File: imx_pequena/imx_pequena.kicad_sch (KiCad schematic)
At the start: 0 parts

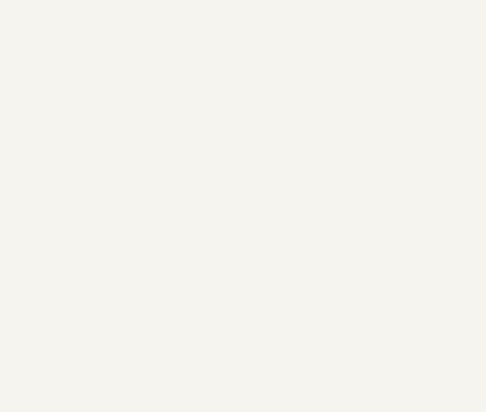
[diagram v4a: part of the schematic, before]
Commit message: Pinout updates
Updated pinout files, changed pinout of gpio 1 and 3
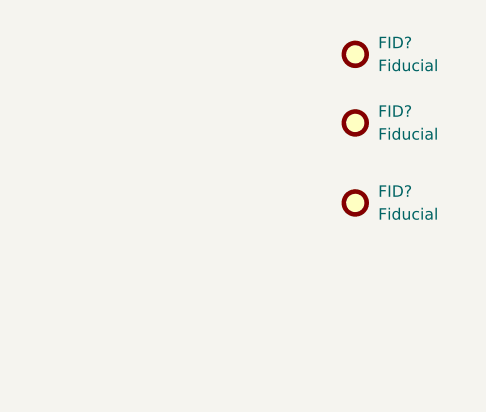
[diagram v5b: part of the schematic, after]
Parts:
- added FID? (x3): Fiducial, symbol Mechanical:Fiducial
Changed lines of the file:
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@@
     (stroke (width 0) (type default) (color 0 0 0 0))
+  )
+  (symbol (lib_id "Mechanical:Fiducial") (at 179.07 77.47 0) (unit 1)
+    (in_bom yes) (on_board yes) (fields_autoplaced)
+    (property "Reference" "FID?" (id 0) (at 181.61 76.1999 0)
+      (effects (font (size 1.27 1.27)) (justify left))
+    )
+    (property "Value" "Fiducial" (id 1) (at 181.61 78.7399 0)
+      (effects (font (size 1.27 1.27)) (justify left))
+    )
+    (property "Footprint" "" (id 2) (at 179.07 77.47 0)
+      (effects (font (size 1.27 1.27)) hide)
+    )
+    (property "Datasheet" "~" (id 3) (at 179.07 77.47 0)
+      (effects (font (size 1.27 1.27)) hide)
+    )
+  )
+  (symbol (lib_id "Mechanical:Fiducial") (at 179.07 86.36 0) (unit 1)
+    (in_bom yes) (on_board yes) (fields_autoplaced)
+    (property "Reference" "FID?" (id 0) (at 181.61 85.0899 0)
+      (effects (font (size 1.27 1.27)) (justify left))
+    )
+    (property "Value" "Fiducial" (id 1) (at 181.61 87.6299 0)
+      (effects (font (size 1.27 1.27)) (justify left))
+    )
+    (property "Footprint" "" (id 2) (at 179.07 86.36 0)
+      (effects (font (size 1.27 1.27)) hide)
+    )
+    (property "Datasheet" "~" (id 3) (at 179.07 86.36 0)
+      (effects (font (size 1.27 1.27)) hide)
+    )
+  )
+  (symbol (lib_id "Mechanical:Fiducial") (at 179.07 69.85 0) (unit 1)
+    (in_bom yes) (on_board yes) (fields_autoplaced)
+    (property "Reference" "FID?" (id 0) (at 181.61 68.5799 0)
+      (effects (font (size 1.27 1.27)) (justify left))
+    )
+    (property "Value" "Fiducial" (id 1) (at 181.61 71.1199 0)
+      (effects (font (size 1.27 1.27)) (justify left))
+    )
+    (property "Footprint" "" (id 2) (at 179.07 69.85 0)
+      (effects (font (size 1.27 1.27)) hide)
+    )
+    (property "Datasheet" "~" (id 3) (at 179.07 69.85 0)
+      (effects (font (size 1.27 1.27)) hide)
+    )
   )
   (sheet (at 54.61 100.33) (size 33.02 20.32) (fields_autoplaced)
@@
       (reference "#PWR?") (unit 1) (value "GND") (footprint "")
     )
+    (path "/e35c56f9-4713-4571-acdb-6ae2f2073fad/19abf78c-447d-4a26-a146-68b25d9e4c7a"
+      (reference "#PWR?") (unit 1) (value "GND") (footprint "")
+    )
     (path "/b1ca3e0b-34ce-4229-a1de-c4269e4ccd13/e4b0b1c3-ef5e-4ab5-8d70-6acfd00108e3/27f72761-f65f-4e29-a308-3170c5b56d4e"
       (reference "#PWR?") (unit 1) (value "GND") (footprint "")
@@
       (reference "D2") (unit 1) (value "D_Schottky") (footprint "")
     )
+    (path "/e35c56f9-4713-4571-acdb-6ae2f2073fad/24569c5c-3905-42a7-b371-b23bc9cdaa9e"
+      (reference "D?") (unit 1) (value "D_TVS") (footprint "")
+    )
     (path "/b1ca3e0b-34ce-4229-a1de-c4269e4ccd13/e4b0b1c3-ef5e-4ab5-8d70-6acfd00108e3/f018a515-bdc2-4719-84b3-f29126a0bfa9"
       (reference "D?") (unit 1) (value "D_Schottky") (footprint "")
@@
       (reference "F?") (unit 1) (value "Fuse_Small") (footprint "")
     )
+    (path "/64e54a22-63a0-4db2-b405-8a28a973ed5d"
+      (reference "FID?") (unit 1) (value "Fiducial") (footprint "")
+    )
+    (path "/b6dfcf66-fbe6-453a-a92a-d4357889378e"
+      (reference "FID?") (unit 1) (value "Fiducial") (footprint "")
+    )
+    (path "/c3797c65-0eba-45f0-a5bc-5a86e83cb0c5"
+      (reference "FID?") (unit 1) (value "Fiducial") (footprint "")
+    )
     (path "/b1ca3e0b-34ce-4229-a1de-c4269e4ccd13/e4b0b1c3-ef5e-4ab5-8d70-6acfd00108e3/af73b285-838d-4b82-83cb-376f8bbe2ef4"
       (reference "J1") (unit 1) (value "Conn_ARM_JTAG_SWD_10") (footprint "")
@@
       (reference "J2") (unit 1) (value "Micro_SD_Card") (footprint "")
     )
-    (path "/e35c56f9-4713-4571-acdb-6ae2f2073fad/f26dfe91-6ea2-4dd7-ac27-80f43cf12e1c"
-      (reference "J3") (unit 1) (value "USB_B_Micro") (footprint "")
-    )
     (path "/e35c56f9-4713-4571-acdb-6ae2f2073fad/e117ef28-5c52-4d5c-bd4e-b5be24785834"
       (reference "J4") (unit 1) (value "USB_C_Receptacle") (footprint "")
     )
+    (path "/e35c56f9-4713-4571-acdb-6ae2f2073fad/b8dbd3c7-4df0-4d11-8ddd-ea24cb3f2676"
+      (reference "J?") (unit 1) (value "USB_A") (footprint "")
+    )
     (path "/08944c63-1cea-4fda-90db-3d649a3edc95/9ee5e8f1-d628-4347-87c6-e91ba1bc0c3e"

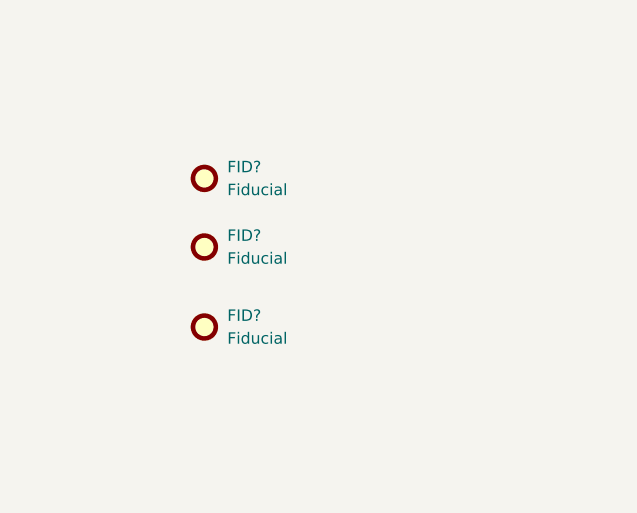
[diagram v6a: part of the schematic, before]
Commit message: Part Assignment
Assigned GPIOs and assigned footprints to most parts
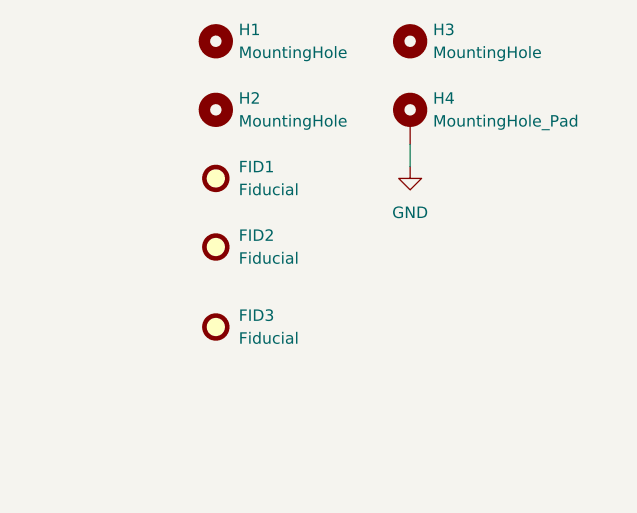
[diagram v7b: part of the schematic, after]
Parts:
- added H1, H2, H3: MountingHole, MountingHole:MountingHole_2.5mm_Pad, symbol Mechanical:MountingHole
- added H4: MountingHole_Pad, MountingHole:MountingHole_2.5mm_Pad, symbol Mechanical:MountingHole_Pad
- FID1, FID2, FID3: renamed from FID?; footprint (none) -> Fiducial:Fiducial_1mm_Mask2mm
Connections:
- new net GND: H4.1
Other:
- moved on the sheet: FID1, FID2, FID3

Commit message: lots of updates
Set design rules, fixed ERC, etc....
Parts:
- H1, H2, H3: footprint MountingHole:MountingHole_2.5mm_Pad -> MountingHole:MountingHole_2.5mm
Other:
- sheet imx_mpu ports: added none; removed I2C2_SCL, I2C2_SDA
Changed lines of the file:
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@@
       (effects (font (size 1.27 1.27)) (justify left))
     )
-    (property "Footprint" "MountingHole:MountingHole_2.5mm_Pad" (id 2) (at 180.34 54.61 0)
+    (property "Footprint" "MountingHole:MountingHole_2.5mm" (id 2) (at 180.34 54.61 0)
       (effects (font (size 1.27 1.27)) hide)
     )
@@
       (effects (font (size 1.27 1.27)) (justify left))
     )
-    (property "Footprint" "MountingHole:MountingHole_2.5mm_Pad" (id 2) (at 201.93 54.61 0)
+    (property "Footprint" "MountingHole:MountingHole_2.5mm" (id 2) (at 201.93 54.61 0)
       (effects (font (size 1.27 1.27)) hide)
     )
@@
       (effects (font (size 1.27 1.27)) (justify left))
     )
-    (property "Footprint" "MountingHole:MountingHole_2.5mm_Pad" (id 2) (at 180.34 62.23 0)
+    (property "Footprint" "MountingHole:MountingHole_2.5mm" (id 2) (at 180.34 62.23 0)
       (effects (font (size 1.27 1.27)) hide)
     )
@@
       (effects (font (size 1.27 1.27)) (justify left top))
     )
-    (pin "I2C2_SCL" bidirectional (at 54.61 73.66 180)
-      (effects (font (size 1.27 1.27)) (justify left))
-    )
     (pin "USB2_DN" bidirectional (at 87.63 88.9 0)
       (effects (font (size 1.27 1.27)) (justify right))
@@
     (pin "USB2_DP" bidirectional (at 87.63 86.36 0)
       (effects (font (size 1.27 1.27)) (justify right))
-    )
-    (pin "I2C2_SDA" bidirectional (at 54.61 71.12 180)
-      (effects (font (size 1.27 1.27)) (justify left))
     )
     (pin "USB1_DN" bidirectional (at 87.63 77.47 0)
@@
     )
     (path "/555d34c4-10d1-48af-95a8-db4f4a4faf49"
-      (reference "H1") (unit 1) (value "MountingHole") (footprint "MountingHole:MountingHole_2.5mm_Pad")
+      (reference "H1") (unit 1) (value "MountingHole") (footprint "MountingHole:MountingHole_2.5mm")
     )
     (path "/c540006f-acfd-4f86-bab2-46f63ae58469"
-      (reference "H2") (unit 1) (value "MountingHole") (footprint "MountingHole:MountingHole_2.5mm_Pad")
+      (reference "H2") (unit 1) (value "MountingHole") (footprint "MountingHole:MountingHole_2.5mm")
     )
     (path "/bfef9c0f-78ab-4444-8284-2ee3a2a1e888"
-      (reference "H3") (unit 1) (value "MountingHole") (footprint "MountingHole:MountingHole_2.5mm_Pad")
+      (reference "H3") (unit 1) (value "MountingHole") (footprint "MountingHole:MountingHole_2.5mm")
     )
     (path "/44b853a4-620e-45a2-9211-899f46761644"
@@
     )
     (path "/b1ca3e0b-34ce-4229-a1de-c4269e4ccd13/e4b0b1c3-ef5e-4ab5-8d70-6acfd00108e3/af73b285-838d-4b82-83cb-376f8bbe2ef4"
-      (reference "J1") (unit 1) (value "Conn_ARM_JTAG_SWD_10") (footprint "Connector_PinHeader_1.27mm:PinHeader_2x05_P1.27mm_Vertical")
+      (reference "J1") (unit 1) (value "Conn_ARM_JTAG_SWD_10") (footprint "")
     )
     (path "/b1ca3e0b-34ce-4229-a1de-c4269e4ccd13/f706b935-d0e8-4efc-a2ee-118b40541d20/5ba73e60-b0ea-4332-960b-b1b75d9138d5"
-      (reference "J2") (unit 1) (value "Micro_SD_Card") (footprint "Connector_Card:microSD_HC_Hirose_DM3AT-SF-PEJM5")
+      (reference "J2") (unit 1) (value "Micro_SD_Card") (footprint "")
     )
     (path "/b1ca3e0b-34ce-4229-a1de-c4269e4ccd13/8547231b-655d-4dc1-90f6-5d7d466e2d62/52654f1a-ab43-4151-9c96-948587e49d47"
@@
     )
     (path "/e35c56f9-4713-4571-acdb-6ae2f2073fad/e117ef28-5c52-4d5c-bd4e-b5be24785834"
-      (reference "J4") (unit 1) (value "USB_C_Receptacle") (footprint "Connector_USB:USB_C_Receptacle_Amphenol_12401610E4-2A_CircularHoles")
+      (reference "J4") (unit 1) (value "USB_C_Receptacle") (footprint "")
     )
     (path "/e35c56f9-4713-4571-acdb-6ae2f2073fad/b8dbd3c7-4df0-4d11-8ddd-ea24cb3f2676"
@@
     )
     (path "/b1ca3e0b-34ce-4229-a1de-c4269e4ccd13/e4b0b1c3-ef5e-4ab5-8d70-6acfd00108e3/7c29cca2-a481-4140-9382-2fdaf3d142da"
-      (reference "Y2") (unit 1) (value "Crystal") (footprint "Crystal:Crystal_SMD_MicroCrystal_MS1V-T1K")
-    )
-  )
+      (reference "Y2") (unit 1) (value "Crystal") (footprint "")
+    )
+  )
